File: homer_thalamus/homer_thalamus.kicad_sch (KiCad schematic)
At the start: 2 parts, among them J1 GPIO

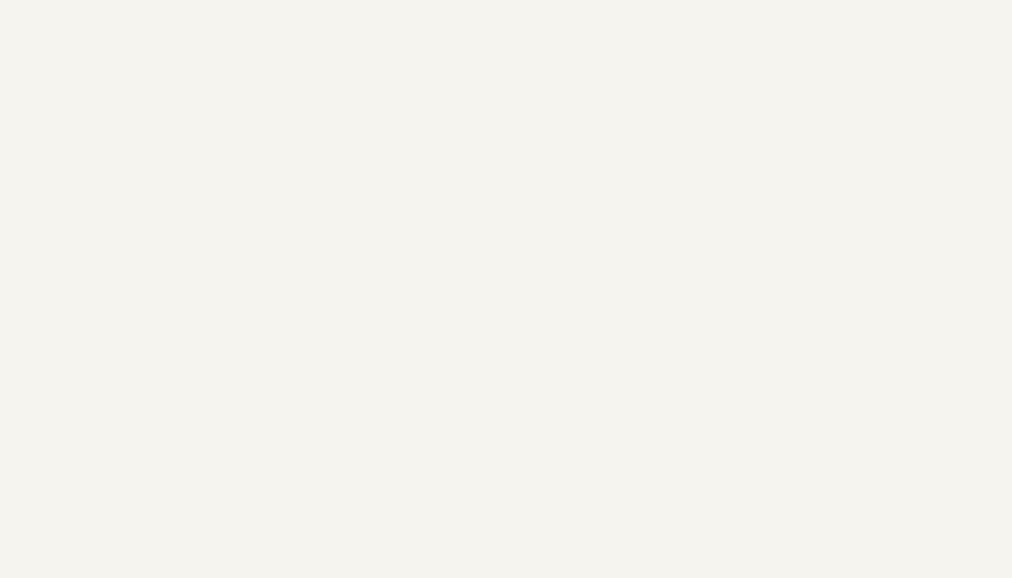
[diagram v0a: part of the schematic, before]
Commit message: start drv8874 carrier footprint
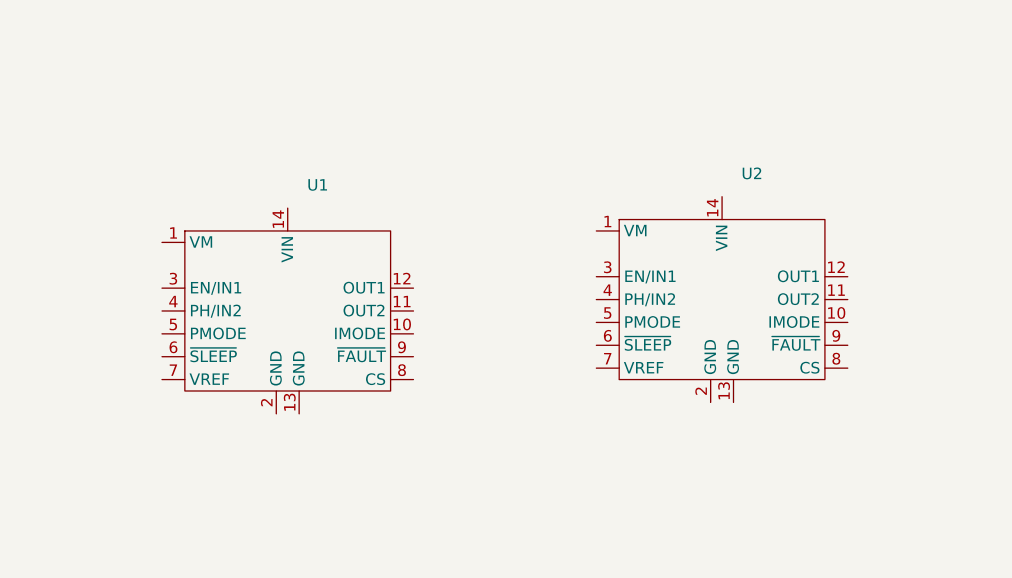
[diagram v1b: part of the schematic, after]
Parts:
- added U1, U2: ~, symbol Pololu_DRV8874_Carrier:DRV8874_Carrier
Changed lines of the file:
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@@
+	)
+	(symbol
+		(lib_id "Pololu_DRV8874_Carrier:DRV8874_Carrier")
+		(at 151.13 125.73 0)
+		(unit 1)
+		(exclude_from_sim no)
+		(in_bom yes)
+		(on_board yes)
+		(dnp no)
+		(fields_autoplaced yes)
+		(property "Reference" "U2"
+			(at 153.2733 111.76 0)
+			(effects
+				(font
+					(size 1.27 1.27)
+				)
+				(justify left)
+			)
+		)
+		(property "Value" "~"
+			(at 153.2733 114.3 0)
+			(effects
+				(font
+					(size 1.27 1.27)
+				)
+				(justify left)
+			)
+		)
+		(property "Footprint" ""
+			(at 146.05 125.73 0)
+			(effects
+				(font
+					(size 1.27 1.27)
+				)
+				(hide yes)
+			)
+		)
+		(property "Datasheet" ""
+			(at 146.05 125.73 0)
+			(effects
+				(font
+					(size 1.27 1.27)
+				)
+				(hide yes)
+			)
+		)
+		(property "Description" ""
+			(at 146.05 125.73 0)
+			(effects
+				(font
+					(size 1.27 1.27)
+				)
+				(hide yes)
+			)
+		)
+		(pin "11"
+		)
+		(pin "9"
+		)
+		(pin "8"
+		)
+		(pin "13"
+		)
+		(pin "3"
+		)
+		(pin "4"
+		)
+		(pin "1"
+		)
+		(pin "12"
+		)
+		(pin "5"
+		)
+		(pin "14"
+		)
+		(pin "6"
+		)
+		(pin "10"
+		)
+		(pin "2"
+		)
+		(pin "7"
+		)
+		(instances
+			(project ""
+				(path "/e63e39d7-6ac0-4ffd-8aa3-1841a4541b55"
+					(reference "U2")
+					(unit 1)
+				)
+			)
+		)
 	)
 	(symbol
@@
 					(unit 1)
 				)
+			)
+		)
+	)
+	(symbol
+		(lib_id "Pololu_DRV8874_Carrier:DRV8874_Carrier")
+		(at 102.87 127 0)
+		(unit 1)
+		(exclude_from_sim no)
+		(in_bom yes)
+		(on_board yes)
+		(dnp no)
+		(fields_autoplaced yes)
+		(property "Reference" "U1"
+			(at 105.0133 113.03 0)
+			(effects
+				(font
+					(size 1.27 1.27)
+				)
+				(justify left)
+			)
+		)
+		(property "Value" "~"
+			(at 105.0133 115.57 0)
+			(effects
+				(font
+					(size 1.27 1.27)
+				)
+				(justify left)
+			)
+		)
+		(property "Footprint" ""
+			(at 97.79 127 0)
+			(effects
+				(font
+					(size 1.27 1.27)
+				)
+				(hide yes)
+			)
+		)
+		(property "Datasheet" ""
+			(at 97.79 127 0)
+			(effects
+				(font
+					(size 1.27 1.27)
+				)
+				(hide yes)
+			)
+		)
+		(property "Description" ""
+			(at 97.79 127 0)
+			(effects
+				(font
+					(size 1.27 1.27)
+				)
+				(hide yes)
+			)
+		)
+		(pin "9"
+		)
+		(pin "8"
+		)
+		(pin "14"
+		)
+		(pin "11"
+		)
+		(pin "2"
+		)
+		(pin "12"
+		)
+		(pin "7"
+		)
+		(pin "6"
+		)
+		(pin "13"
+		)
+		(pin "1"
+		)
+		(pin "4"
+		)
+		(pin "5"
+		)
+		(pin "10"
+		)
+		(pin "3"
+		)
+		(instances
+			(project ""
+				(path "/e63e39d7-6ac0-4ffd-8aa3-1841a4541b55"
+					(reference "U1")
+					(unit 1)
+				)

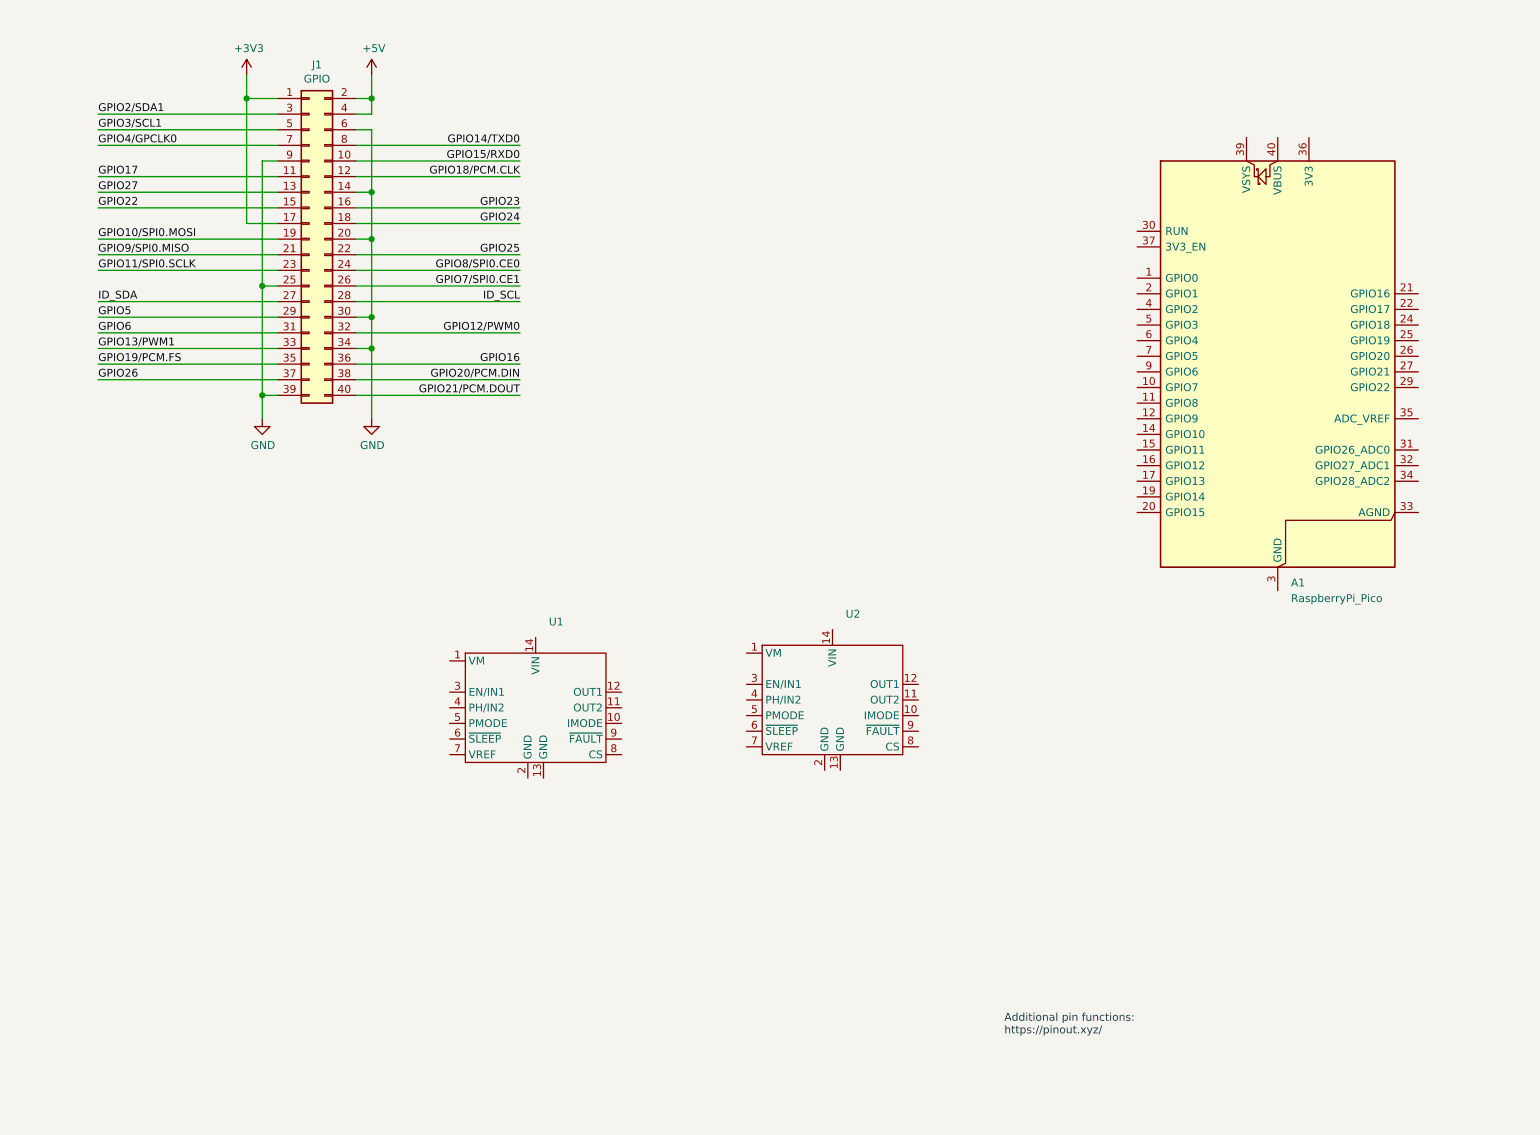
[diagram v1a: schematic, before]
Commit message: add peripherals
- Button
- RGB LED
- HC-SR04
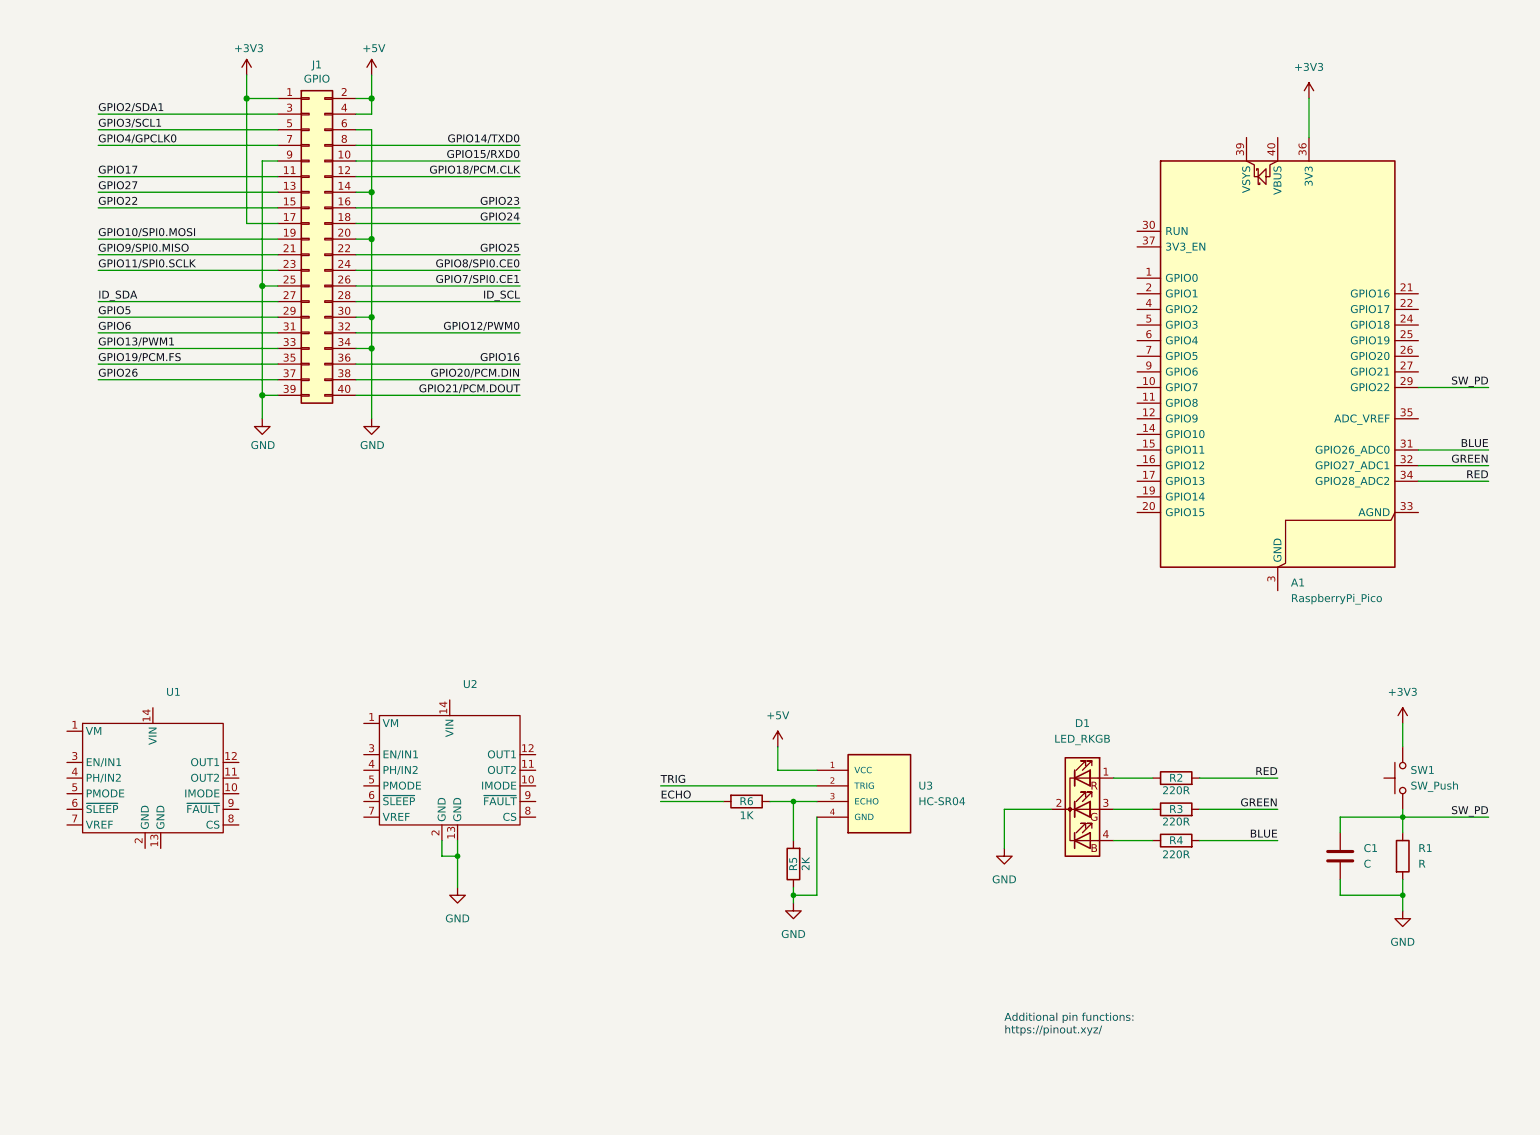
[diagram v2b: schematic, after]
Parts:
- added C1: C, symbol Device:C
- added D1: LED_RKGB, symbol Device:LED_RKGB
- added R1: R, symbol Device:R
- added R2, R3, R4: 220R, symbol Device:R
- added R5: 2K, symbol Device:R
- added R6: 1K, symbol Device:R
- added SW1: SW_Push, symbol Switch:SW_Push
- added U3: HC-SR04, HC-SR04:XCVR_HC-SR04, symbol HC-SR04:HC-SR04
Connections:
- net +3V3: now also A1.36 (3V3), SW1.2
- net +5V: now also U3.1 (VCC)
- net GND: now also U2.13 (GND), U2.2 (GND), C1.2, D1.2 (K), R1.2, R5.1, U3.4 (GND)
- net SW_PD: now reaches A1.29 (GPIO22)
- net SW_PD: now also C1.1, R1.1, SW1.1
- net BLUE: now reaches A1.31 (GPIO26_ADC0)
- net BLUE: now also R4.2
- net GREEN: now reaches A1.32 (GPIO27_ADC1)
- net GREEN: now also R3.2
- net RED: now reaches A1.34 (GPIO28_ADC2)
- net RED: now also R2.2
- new net: D1.1 (RA), R2.1
- new net: D1.3 (GA), R3.1
- new net: D1.4 (BA), R4.1
- new net: R5.2, R6.1, U3.3 (ECHO)
- new net ECHO: R6.2
- new net TRIG: U3.2 (TRIG)
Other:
- moved on the sheet: U1, U2

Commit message: update motor driving and sensing section
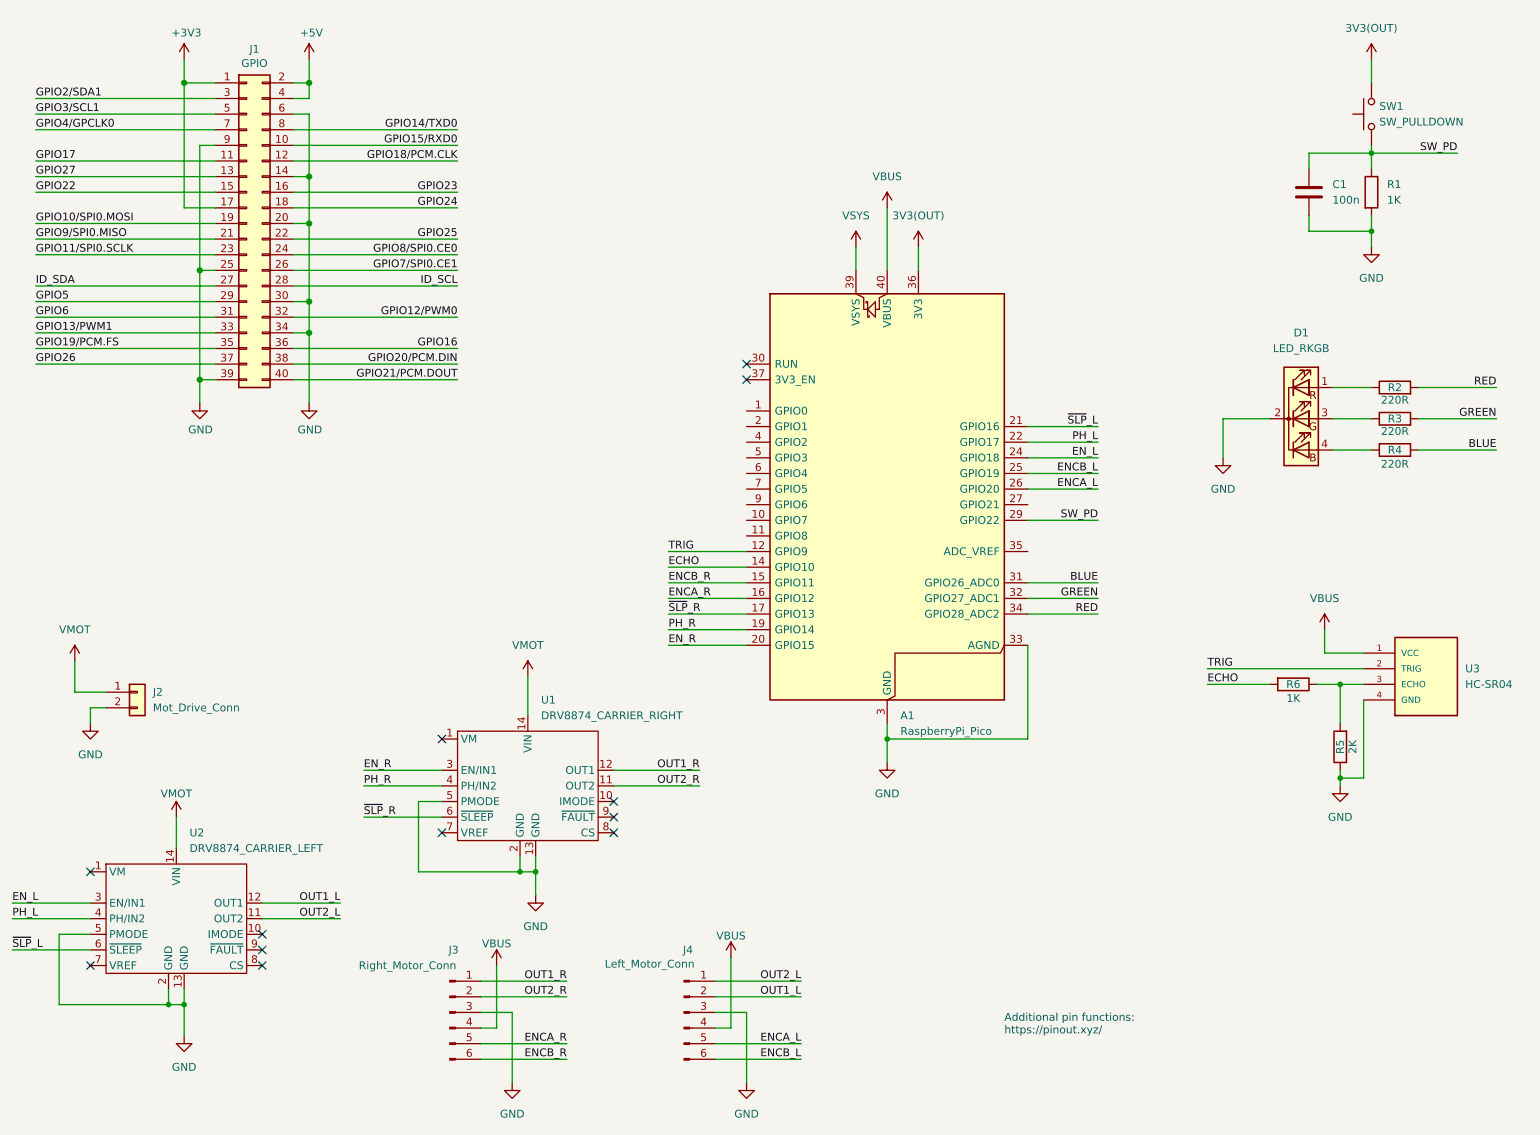
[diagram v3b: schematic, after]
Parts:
- added J2: Mot_Drive_Conn, symbol Connector_Generic:Conn_01x02
- added J3: Right_Motor_Conn, symbol Connector:Conn_01x06_Pin
- added J4: Left_Motor_Conn, symbol Connector:Conn_01x06_Pin
- C1: value C -> 100n
- R1: value R -> 1K
- SW1: value SW_Push -> SW_PULLDOWN
- U1: value ~ -> DRV8874_CARRIER_RIGHT
- U2: value ~ -> DRV8874_CARRIER_LEFT
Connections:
- net +3V3: no longer A1.36 (3V3), SW1.2
- net +5V: no longer U3.1 (VCC)
- net ECHO: now also A1.14 (GPIO10)
- net GND: now also A1.13 (GND), A1.18 (GND), A1.23 (GND), A1.28 (GND), A1.3 (GND), A1.33 (AGND), A1.38 (GND), A1.8 (GND), U1.13 (GND), U1.2 (GND), U1.5 (PMODE), U2.5 (PMODE), J2.2 (Pin_2), J3.3 (Pin_3), J4.3 (Pin_3)
- net TRIG: now also A1.12 (GPIO9)
- net OUT2_L: now reaches U2.11 (OUT2)
- net OUT2_L: now also J4.1 (Pin_1)
- net OUT1_L: now reaches U2.12 (OUT1)
- net OUT1_L: now also J4.2 (Pin_2)
- net VMOT: now reaches U2.14 (VIN)
- net VMOT: now also U1.14 (VIN), J2.1 (Pin_1)
- net EN_L: now reaches U2.3 (EN/IN1)
- net EN_L: now also A1.24 (GPIO18)
- net PH_L: now reaches U2.4 (PH/IN2)
- net PH_L: now also A1.22 (GPIO17)
- net ~{SLP}_L: now reaches U2.6 (~{SLEEP})
- net ~{SLP}_L: now also A1.21 (GPIO16)
- net ENCB_R: now reaches A1.15 (GPIO11)
- net ENCB_R: now also J3.6 (Pin_6)
- net ENCA_R: now reaches A1.16 (GPIO12)
- net ENCA_R: now also J3.5 (Pin_5)
- net ~{SLP}_R: now reaches A1.17 (GPIO13)
- net ~{SLP}_R: now also U1.6 (~{SLEEP})
- net PH_R: now reaches A1.19 (GPIO14)
- net PH_R: now also U1.4 (PH/IN2)
- net EN_R: now reaches A1.20 (GPIO15)
- net EN_R: now also U1.3 (EN/IN1)
- net ENCB_L: now reaches A1.25 (GPIO19)
- net ENCB_L: now also J4.6 (Pin_6)
- net ENCA_L: now reaches A1.26 (GPIO20)
- net ENCA_L: now also J4.5 (Pin_5)
- net VSYS: now reaches A1.39 (VSYS)
- net VBUS: now reaches A1.40 (VBUS)
- net VBUS: now also U3.1 (VCC), J3.4 (Pin_4), J4.4 (Pin_4)
- net OUT2_R: now reaches U1.11 (OUT2)
- net OUT2_R: now also J3.2 (Pin_2)
- net OUT1_R: now reaches U1.12 (OUT1)
- net OUT1_R: now also J3.1 (Pin_1)
- new net 3V3(OUT): A1.36 (3V3), SW1.2
- no-connect marks 0 -> 12
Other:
- company: (none) -> Engineering Physics - UCA
- title: (none) -> Homer Thalamus
- moved on the sheet: A1, C1, D1, J1, R1, R2, R3, R4, R5, R6, SW1, U1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
